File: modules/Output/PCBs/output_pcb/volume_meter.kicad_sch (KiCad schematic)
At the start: 41 parts, among them U10 TL074, U11 TL074, U12 TL074

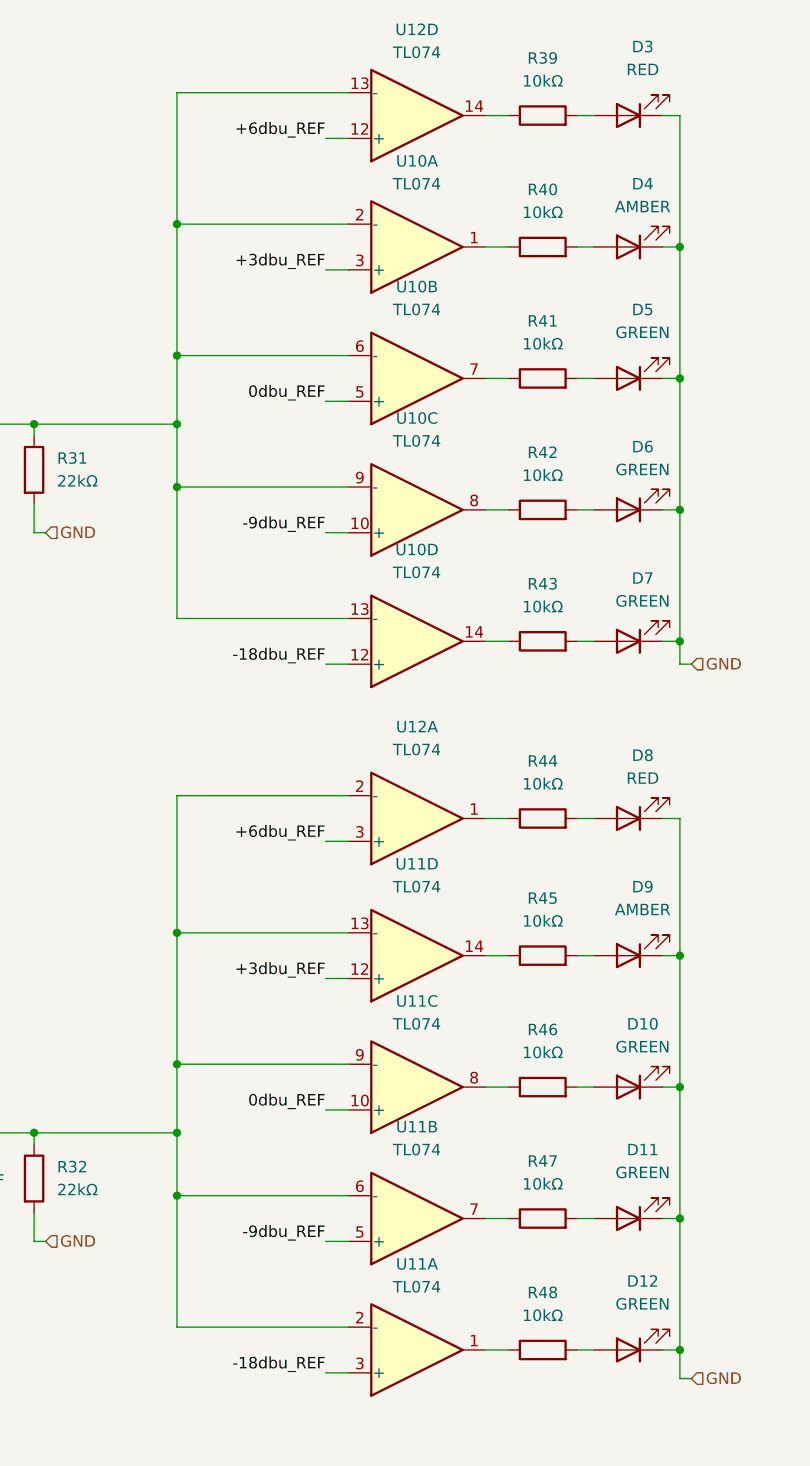
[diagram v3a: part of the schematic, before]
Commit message: Fix errors in output PCB
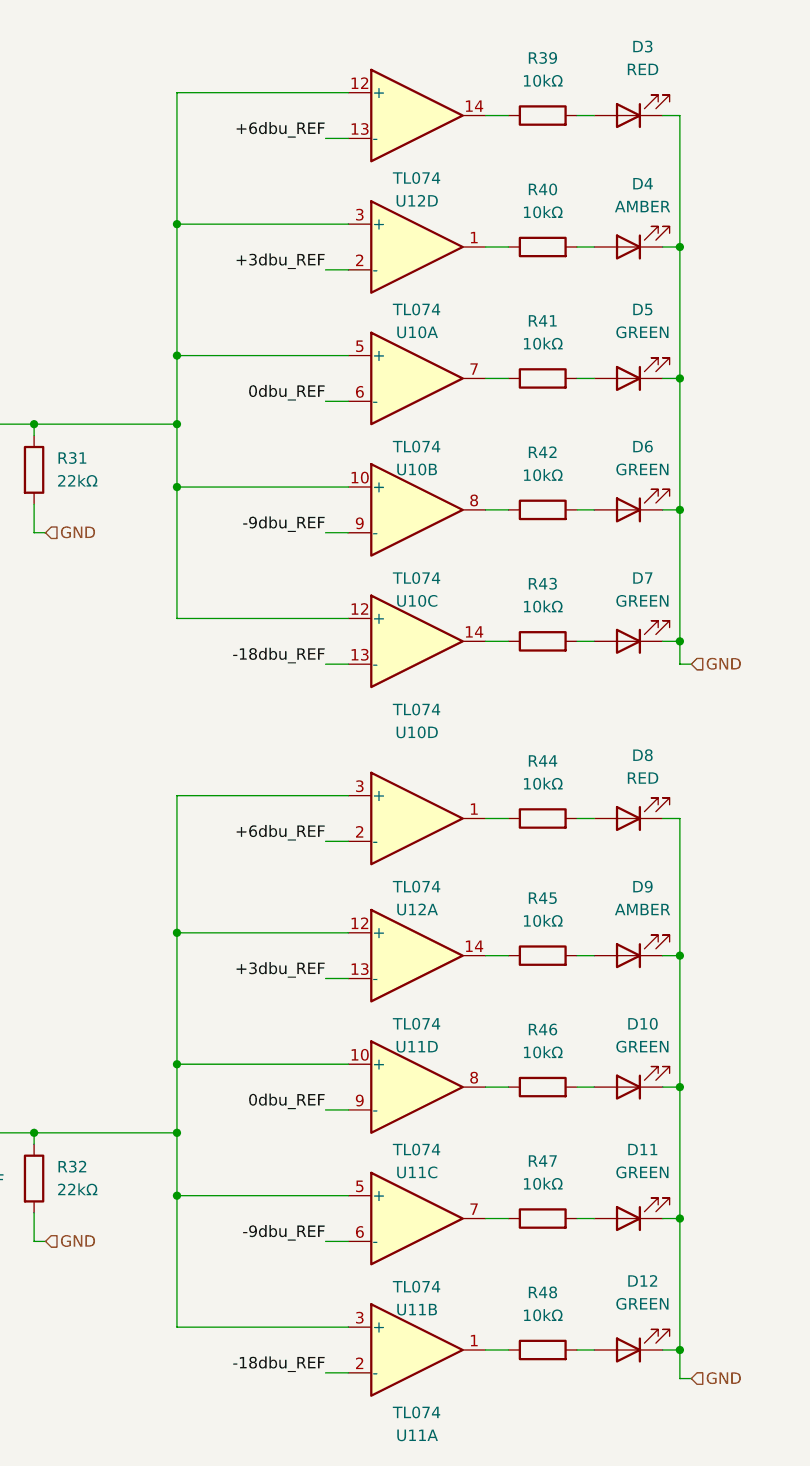
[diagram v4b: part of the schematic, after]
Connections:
- net +3dbu_REF: now also U10.2 (-), U11.13 (-); no longer U10.3 (+), U11.12 (+)
- net +6dbu_REF: now also U12.13 (-), U12.2 (-); no longer U12.12 (+), U12.3 (+)
- net -18dbu_REF: now also U10.13 (-), U11.2 (-); no longer U10.12 (+), U11.3 (+)
- net -9dbu_REF: now also U10.9 (-), U11.6 (-); no longer U10.10 (+), U11.5 (+)
- net 0dbu_REF: now also U10.6 (-), U11.9 (-); no longer U10.5 (+), U11.10 (+)
- new net: C32.1, D1.1 (K), R31.1, U10.10 (+), U10.12 (+), U10.3 (+), U10.5 (+), U12.12 (+), U12.9 (-)
- new net: C31.1, D2.1 (K), R32.1, U11.10 (+), U11.12 (+), U11.3 (+), U11.5 (+), U12.3 (+), U12.6 (-)
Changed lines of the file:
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@@
 		(lib_id "Amplifier_Operational:TL074")
 		(at 128.27 26.67 0)
-		(mirror x)
 		(unit 4)
 		(exclude_from_sim no)
@@
 		(dnp no)
 		(property "Reference" "U12"
-			(at 128.27 17.145 0)
+			(at 128.27 36.195 0)
 			(effects
 				(font
@@
 		)
 		(property "Value" "TL074"
-			(at 128.27 19.685 0)
+			(at 128.27 33.655 0)
 			(effects
 				(font
@@
 		)
 		(property "Footprint" "Package_DIP:DIP-14_W7.62mm"
-			(at 127 29.21 0)
+			(at 127 24.13 0)
 			(effects
 				(font
@@
 		)
 		(property "Datasheet" "http://www.ti.com/lit/ds/symlink/tl071.pdf"
-			(at 129.54 31.75 0)
+			(at 129.54 21.59 0)
 			(effects
 				(font
@@
 		(lib_id "Amplifier_Operational:TL074")
 		(at 128.27 120.015 0)
-		(mirror x)
 		(unit 4)
 		(exclude_from_sim no)
@@
 		(on_board yes)
 		(dnp no)
-		(fields_autoplaced yes)
 		(property "Reference" "U11"
-			(at 128.27 109.855 0)
+			(at 128.27 130.175 0)
 			(effects
 				(font
@@
 		)
 		(property "Value" "TL074"
-			(at 128.27 112.395 0)
+			(at 128.27 127.635 0)
 			(effects
 				(font
@@
 		)
 		(property "Footprint" "Package_DIP:DIP-14_W7.62mm"
-			(at 127 122.555 0)
+			(at 127 117.475 0)
 			(effects
 				(font
@@
 		)
 		(property "Datasheet" "http://www.ti.com/lit/ds/symlink/tl071.pdf"
-			(at 129.54 125.095 0)
+			(at 129.54 114.935 0)
 			(effects
 				(font
@@
 		(lib_id "Amplifier_Operational:TL074")
 		(at 128.27 70.485 0)
-		(mirror x)
 		(unit 3)
 		(exclude_from_sim no)
@@
 		(on_board yes)
 		(dnp no)
-		(fields_autoplaced yes)
 		(property "Reference" "U10"
-			(at 128.27 60.325 0)
+			(at 128.27 80.645 0)
 			(effects
 				(font
@@
 		)
 		(property "Value" "TL074"
-			(at 128.27 62.865 0)
+			(at 128.27 78.105 0)
 			(effects
 				(font
@@
 		)
 		(property "Footprint" "Package_DIP:DIP-14_W7.62mm"
-			(at 127 73.025 0)
+			(at 127 67.945 0)
 			(effects
 				(font
@@
 		)
 		(property "Datasheet" "http://www.ti.com/lit/ds/symlink/tl071.pdf"
-			(at 129.54 75.565 0)
+			(at 129.54 65.405 0)
 			(effects
 				(font
@@
 		(lib_id "Amplifier_Operational:TL074")
 		(at 128.27 55.88 0)
-		(mirror x)
 		(unit 2)
 		(exclude_from_sim no)
@@
 		(on_board yes)
 		(dnp no)
-		(fields_autoplaced yes)
 		(property "Reference" "U10"
-			(at 128.27 45.72 0)
+			(at 128.27 66.04 0)
 			(effects
 				(font
@@
 		)
 		(property "Value" "TL074"
-			(at 128.27 48.26 0)
+			(at 128.27 63.5 0)
 			(effects
 				(font
@@
 		)
 		(property "Footprint" "Package_DIP:DIP-14_W7.62mm"
-			(at 127 58.42 0)
+			(at 127 53.34 0)
 			(effects
 				(font
@@
 		)
 		(property "Datasheet" "http://www.ti.com/lit/ds/symlink/tl071.pdf"
-			(at 129.54 60.96 0)
+			(at 129.54 50.8 0)
 			(effects
 				(font
@@
 		(lib_id "Amplifier_Operational:TL074")
 		(at 128.27 149.225 0)
-		(mirror x)
 		(unit 2)
 		(exclude_from_sim no)
@@
 		(on_board yes)
 		(dnp no)
-		(fields_autoplaced yes)
 		(property "Reference" "U11"
-			(at 128.27 139.065 0)
+			(at 128.27 159.385 0)
 			(effects
 				(font
@@
 		)
 		(property "Value" "TL074"
-			(at 128.27 141.605 0)
+			(at 128.27 156.845 0)
 			(effects
 				(font
@@
 		)
 		(property "Footprint" "Package_DIP:DIP-14_W7.62mm"
-			(at 127 151.765 0)
+			(at 127 146.685 0)
 			(effects
 				(font
@@
 		)
 		(property "Datasheet" "http://www.ti.com/lit/ds/symlink/tl071.pdf"
-			(at 129.54 154.305 0)
+			(at 129.54 144.145 0)
 			(effects
 				(font
@@
 		(lib_id "Amplifier_Operational:TL074")
 		(at 128.27 134.62 0)
-		(mirror x)
 		(unit 3)
 		(exclude_from_sim no)
@@
 		(on_board yes)
 		(dnp no)
-		(fields_autoplaced yes)
 		(property "Reference" "U11"
-			(at 128.27 125.095 0)
+			(at 128.27 144.145 0)
 			(effects
 				(font
@@
 		)
 		(property "Value" "TL074"
-			(at 128.27 127.635 0)
+			(at 128.27 141.605 0)
 			(effects
 				(font
@@
 		)
 		(property "Footprint" "Package_DIP:DIP-14_W7.62mm"
-			(at 127 137.16 0)
+			(at 127 132.08 0)
 			(effects
 				(font
@@
 		)
 		(property "Datasheet" "http://www.ti.com/lit/ds/symlink/tl071.pdf"
-			(at 129.54 139.7 0)
+			(at 129.54 129.54 0)
 			(effects
 				(font
@@
 		(lib_id "Amplifier_Operational:TL074")
 		(at 128.27 163.83 0)
-		(mirror x)
 		(unit 1)
 		(exclude_from_sim no)
@@
 		(on_board yes)
 		(dnp no)
-		(fields_autoplaced yes)
 		(property "Reference" "U11"
-			(at 128.27 154.305 0)
+			(at 128.27 173.355 0)
 			(effects
 				(font
@@
 		)
 		(property "Value" "TL074"
-			(at 128.27 156.845 0)
+			(at 128.27 170.815 0)
 			(effects
 				(font
@@
 		)
 		(property "Footprint" "Package_DIP:DIP-14_W7.62mm"
-			(at 127 166.37 0)
+			(at 127 161.29 0)
 			(effects
 				(font
@@
 		)
 		(property "Datasheet" "http://www.ti.com/lit/ds/symlink/tl071.pdf"
-			(at 129.54 168.91 0)
+			(at 129.54 158.75 0)
 			(effects
 				(font
@@
 		(lib_id "Amplifier_Operational:TL074")
 		(at 128.27 85.09 0)
-		(mirror x)
 		(unit 4)
 		(exclude_from_sim no)
@@
 		(on_board yes)
 		(dnp no)
-		(fields_autoplaced yes)
 		(property "Reference" "U10"
-			(at 128.27 74.93 0)
+			(at 128.27 95.25 0)
 			(effects
 				(font
@@
 		)
 		(property "Value" "TL074"
-			(at 128.27 77.47 0)
+			(at 128.27 92.71 0)
 			(effects
 				(font
@@
 		)
 		(property "Footprint" "Package_DIP:DIP-14_W7.62mm"
-			(at 127 87.63 0)
+			(at 127 82.55 0)
 			(effects
 				(font
@@
 		)
 		(property "Datasheet" "http://www.ti.com/lit/ds/symlink/tl071.pdf"
-			(at 129.54 90.17 0)
+			(at 129.54 80.01 0)
 			(effects
 				(font
@@
 		(lib_id "Amplifier_Operational:TL074")
 		(at 128.27 104.775 0)
-		(mirror x)
 		(unit 1)
 		(exclude_from_sim no)
@@
 		(on_board yes)
 		(dnp no)
-		(fields_autoplaced yes)
 		(property "Reference" "U12"
-			(at 128.27 94.615 0)
+			(at 128.27 114.935 0)
 			(effects
 				(font
@@
 		)
 		(property "Value" "TL074"
-			(at 128.27 97.155 0)
+			(at 128.27 112.395 0)
 			(effects
 				(font
@@
 		)
 		(property "Footprint" "Package_DIP:DIP-14_W7.62mm"
-			(at 127 107.315 0)
+			(at 127 102.235 0)
 			(effects
 				(font
@@
 		)
 		(property "Datasheet" "http://www.ti.com/lit/ds/symlink/tl071.pdf"
-			(at 129.54 109.855 0)
+			(at 129.54 99.695 0)
 			(effects
 				(font
@@
 		(lib_id "Amplifier_Operational:TL074")
 		(at 128.27 41.275 0)
-		(mirror x)
 		(unit 1)
 		(exclude_from_sim no)
@@
 		(on_board yes)
 		(dnp no)
-		(fields_autoplaced yes)
 		(property "Reference" "U10"
-			(at 128.27 31.75 0)
+			(at 128.27 50.8 0)
 			(effects
 				(font
@@
 		)
 		(property "Value" "TL074"
-			(at 128.27 34.29 0)
+			(at 128.27 48.26 0)
 			(effects
 				(font
@@
 		)
 		(property "Footprint" "Package_DIP:DIP-14_W7.62mm"
-			(at 127 43.815 0)
+			(at 127 38.735 0)
 			(effects
 				(font
@@
 		)
 		(property "Datasheet" "http://www.ti.com/lit/ds/symlink/tl071.pdf"
-			(at 129.54 46.355 0)
+			(at 129.54 36.195 0)
 			(effects
 				(font
